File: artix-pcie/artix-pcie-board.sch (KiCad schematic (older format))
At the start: 2 parts, among them U1 xc7a15tfgg484, U2 TOFE-4X

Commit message: added qspi flash. need jtag connector next
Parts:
- added U3: N25Q256_QSPI, footlib:micron_SOP2-16, symbol N25Q256_QSPI
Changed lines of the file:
@@
 Wire Wire Line
 	7100 7600 7500 7600
+$Comp
+L N25Q256_QSPI U3
+U 1 1 568326FE
+P 14000 8100
+F 0 "U3" H 13975 8703 60  0000 C CNN
+F 1 "N25Q256_QSPI" H 13975 8597 60  0000 C CNN
+F 2 "footlib:micron_SOP2-16" H 14000 8100 60  0001 C CNN
+F 3 "" H 14000 8100 60  0000 C CNN
+	1    14000 8100
+	1    0    0    -1
+$EndComp
 $EndSCHEMATC

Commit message: added jtag connector. consider CSG325 17x17mm package
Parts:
- added P1: JTAG_CONN, footlib:JTAG_RA, symbol JTAG_CONN
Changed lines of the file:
@@
+	1    0    0    -1
+$EndComp
+$Comp
+L JTAG_CONN P1
+U 1 1 56833A6D
+P 12950 6700
+F 0 "P1" H 12975 7203 60  0000 C CNN
+F 1 "JTAG_CONN" H 12975 7097 60  0000 C CNN
+F 2 "footlib:JTAG_RA" H 12950 6700 60  0001 C CNN
+F 3 "" H 12950 6700 60  0000 C CNN
+	1    12950 6700
 	1    0    0    -1
 $EndComp

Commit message: working on 0.8mm BGA problem
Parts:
- added U4: AD9361, footlib:AD9361, symbol AD9361
- added U5: xc7a15tcsg325, footlib:Xil_Artix_CSG325, symbol xc7a15tcsg325
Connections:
- wire segments 40 -> 41
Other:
- moved on the sheet: P1, U1A, U1B, U1C, U1D, U1E, U1F, U1G, U1H, U1I, U2, U3

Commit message: wiring PCIe
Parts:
- removed P1: JTAG_CONN, footlib:JTAG_RA, symbol JTAG_CONN
- removed U1: xc7a15tfgg484, footlib:Xil_Artix_BGA_484, symbol xc7a15tfgg484
- removed U2: TOFE-4X, footlib:Xil_Artix_BGA_484, symbol TOFE-4X
- removed U3: N25Q256_QSPI, footlib:micron_SOP2-16, symbol N25Q256_QSPI
- removed U4: AD9361, footlib:AD9361, symbol AD9361
- removed U5: xc7a15tcsg325, footlib:Xil_Artix_CSG325, symbol xc7a15tcsg325
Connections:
- net labels removed: 12V, 3V3, GND, V2_5
- wire segments 41 -> 0
- no-connect marks 1 -> 0

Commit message: working the hierarchy
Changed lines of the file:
@@
 EESchema Schematic File Version 2
+LIBS:artix-pcie-board-rescue
 LIBS:TOFE
 LIBS:xilinx7
@@
 $EndDescr
 $Sheet
-S 7650 1800 1600 1700
+S 3150 2300 1650 2500
 U 568574A3
 F0 "Sheet568574A2" 60
 F1 "fpga.sch" 60
+F2 "PETp0" I R 4800 3850 60
+F3 "PETn0" I R 4800 3950 60
+F4 "PETp1" I R 4800 4100 60
+F5 "PETn1" I R 4800 4200 60
+F6 "PETp2" I R 4800 4350 60
+F7 "PETn2" I R 4800 4450 60
+F8 "PETp3" I R 4800 4600 60
+F9 "PETn3" I R 4800 4700 60
+F10 "REFCLK+" I R 4800 2600 60
+F11 "REFCLK-" I R 4800 2700 60
+F12 "PERp0" O R 4800 2850 60
+F13 "PERn0" O R 4800 2950 60
+F14 "PERp1" O R 4800 3100 60
+F15 "PERn1" O R 4800 3200 60
+F16 "PERp2" O R 4800 3350 60
+F17 "PERn2" O R 4800 3450 60
+F18 "PERp3" O R 4800 3600 60
+F19 "PERn3" O R 4800 3700 60
+F20 "PERST#" I R 4800 2400 60
 $EndSheet
 $Sheet
-S 2450 5150 1950 1700
+S 5950 2300 1000 2500
 U 5685901C
 F0 "Sheet5685901B" 60
 F1 "pcie.sch" 60
+F2 "12V" O R 6950 2400 60
+F3 "GND" O R 6950 2600 60
+F4 "REFCLK+" O L 5950 2600 60
+F5 "REFCLK-" O L 5950 2700 60
+F6 "PETp0" O L 5950 3850 60
+F7 "PETn0" O L 5950 3950 60
+F8 "PETp1" O L 5950 4100 60
+F9 "PETn1" O L 5950 4200 60
+F10 "PETp2" O L 5950 4350 60
+F11 "PETn2" O L 5950 4450 60
+F12 "PETp3" O L 5950 4600 60
+F13 "PETn3" O L 5950 4700 60
+F14 "PERp0" I L 5950 2850 60
+F15 "PERn0" I L 5950 2950 60
+F16 "PERp1" I L 5950 3100 60
+F17 "PERn1" I L 5950 3200 60
+F18 "PERp2" I L 5950 3350 60
+F19 "PERn2" I L 5950 3450 60
+F20 "PERp3" I L 5950 3600 60
+F21 "PERn3" I L 5950 3700 60
+F22 "PERST#" O L 5950 2400 60
 $EndSheet
 $Sheet
-S 2350 1800 1250 1550
+S 7900 2300 1250 1550
 U 56859894
 F0 "Sheet56859893" 60
 F1 "power.sch" 60
 $EndSheet
+Wire Wire Line
+	4800 2400 5950 2400
+Wire Wire Line
+	5950 2600 4800 2600
+Wire Wire Line
+	4800 2700 5950 2700
+Wire Wire Line
+	5950 2850 4800 2850
+Wire Wire Line
+	4800 2950 5950 2950
+Wire Wire Line
+	5950 3100 4800 3100
+Wire Wire Line
+	4800 3200 5950 3200
+Wire Wire Line
+	4800 3350 5950 3350
+Wire Wire Line
+	5950 3450 4800 3450
+Wire Wire Line
+	4800 3600 5950 3600
+Wire Wire Line
+	5950 3700 4800 3700
+Wire Wire Line
+	4800 3850 5950 3850
+Wire Wire Line
+	5950 3950 4800 3950
+Wire Wire Line
+	4800 4100 5950 4100
+Wire Wire Line
+	5950 4200 4800 4200
+Wire Wire Line
+	4800 4350 5950 4350
+Wire Wire Line
+	5950 4450 4800 4450
+Wire Wire Line
+	4800 4600 5950 4600
+Wire Wire Line
+	5950 4700 4800 4700
+Text Label 5000 2400 0    60   ~ 0
+pcie_PERST#
+Text Label 5000 2600 0    60   ~ 0
+pcie_REFCLK+
+Text Label 5000 2700 0    60   ~ 0
+pcie_REFCLK-
+Text Label 5000 2850 0    60   ~ 0
+pcie_PERp0
+Text Label 5000 2950 0    60   ~ 0
+pcie_PERn0
+Text Label 5000 3100 0    60   ~ 0
+pcie_PERp1
+Text Label 5000 3350 0    60   ~ 0
+pcie_PERp2
+Text Label 5000 3600 0    60   ~ 0
+pcie_PERp3
+Text Label 5000 3850 0    60   ~ 0
+pcie_PETp0
+Text Label 5000 3950 0    60   ~ 0
+pcie_PETn0
+Text Label 5000 3200 0    60   ~ 0
+pcie_PERn1
+Text Label 5000 3450 0    60   ~ 0
+pcie_PERn2
+Text Label 5000 3700 0    60   ~ 0
+pcie_PERn3
+Text Label 5000 4100 0    60   ~ 0
+pcie_PETp1
+Text Label 5000 4350 0    60   ~ 0
+pcie_PETp2
+Text Label 5000 4600 0    60   ~ 0
+pcie_PETp3
+Text Label 5000 4200 0    60   ~ 0
+pcie_PETn1
+Text Label 5000 4450 0    60   ~ 0
+pcie_PETn2
+Text Label 5000 4700 0    60   ~ 0
+pcie_PETn3
 $EndSCHEMATC

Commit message: thinking about power supplies
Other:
- note added: "TODO\n- PMODS\n- Oscillator\n- LEDs"
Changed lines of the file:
@@
 Text Label 5000 4700 0    60   ~ 0
 pcie_PETn3
+Text Notes 900  6550 0    60   ~ 0
+TODO\n- PMODS\n- Oscillator\n- LEDs
 $EndSCHEMATC

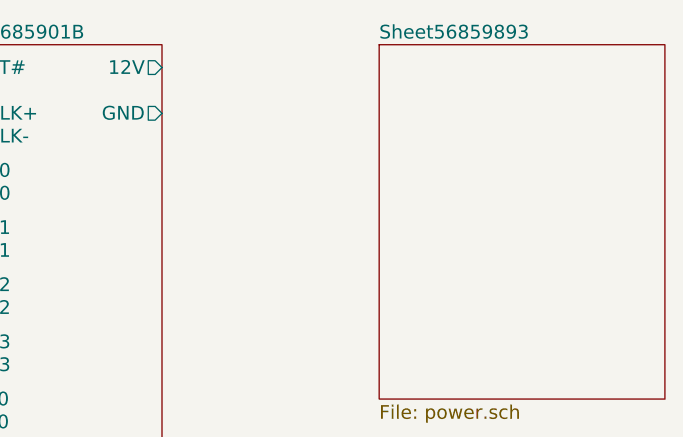
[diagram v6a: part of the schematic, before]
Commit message: fpga compiles and reports power. need to add pmod, oscillator and power supply
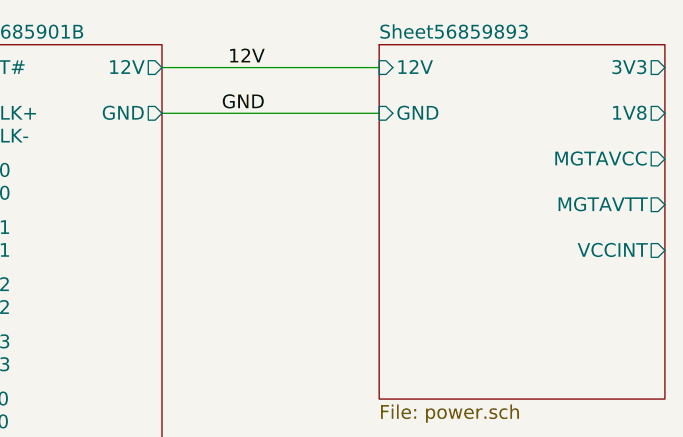
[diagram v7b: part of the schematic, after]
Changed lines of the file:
@@
 F0 "Sheet56859893" 60
 F1 "power.sch" 60
+F2 "12V" I L 7900 2400 60
+F3 "GND" I L 7900 2600 60
+F4 "3V3" O R 9150 2400 60
+F5 "1V8" O R 9150 2600 60
+F6 "MGTAVCC" O R 9150 2800 60
+F7 "MGTAVTT" O R 9150 3000 60
+F8 "VCCINT" O R 9150 3200 60
 $EndSheet
 Wire Wire Line
@@
 Text Notes 900  6550 0    60   ~ 0
 TODO\n- PMODS\n- Oscillator\n- LEDs
+Wire Wire Line
+	7900 2400 6950 2400
+Wire Wire Line
+	6950 2600 7900 2600
+Text Label 7400 2400 2    60   ~ 0
+12V
+Text Label 7400 2600 2    60   ~ 0
+GND
 $EndSCHEMATC
